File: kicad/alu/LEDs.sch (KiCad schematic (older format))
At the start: 114 parts

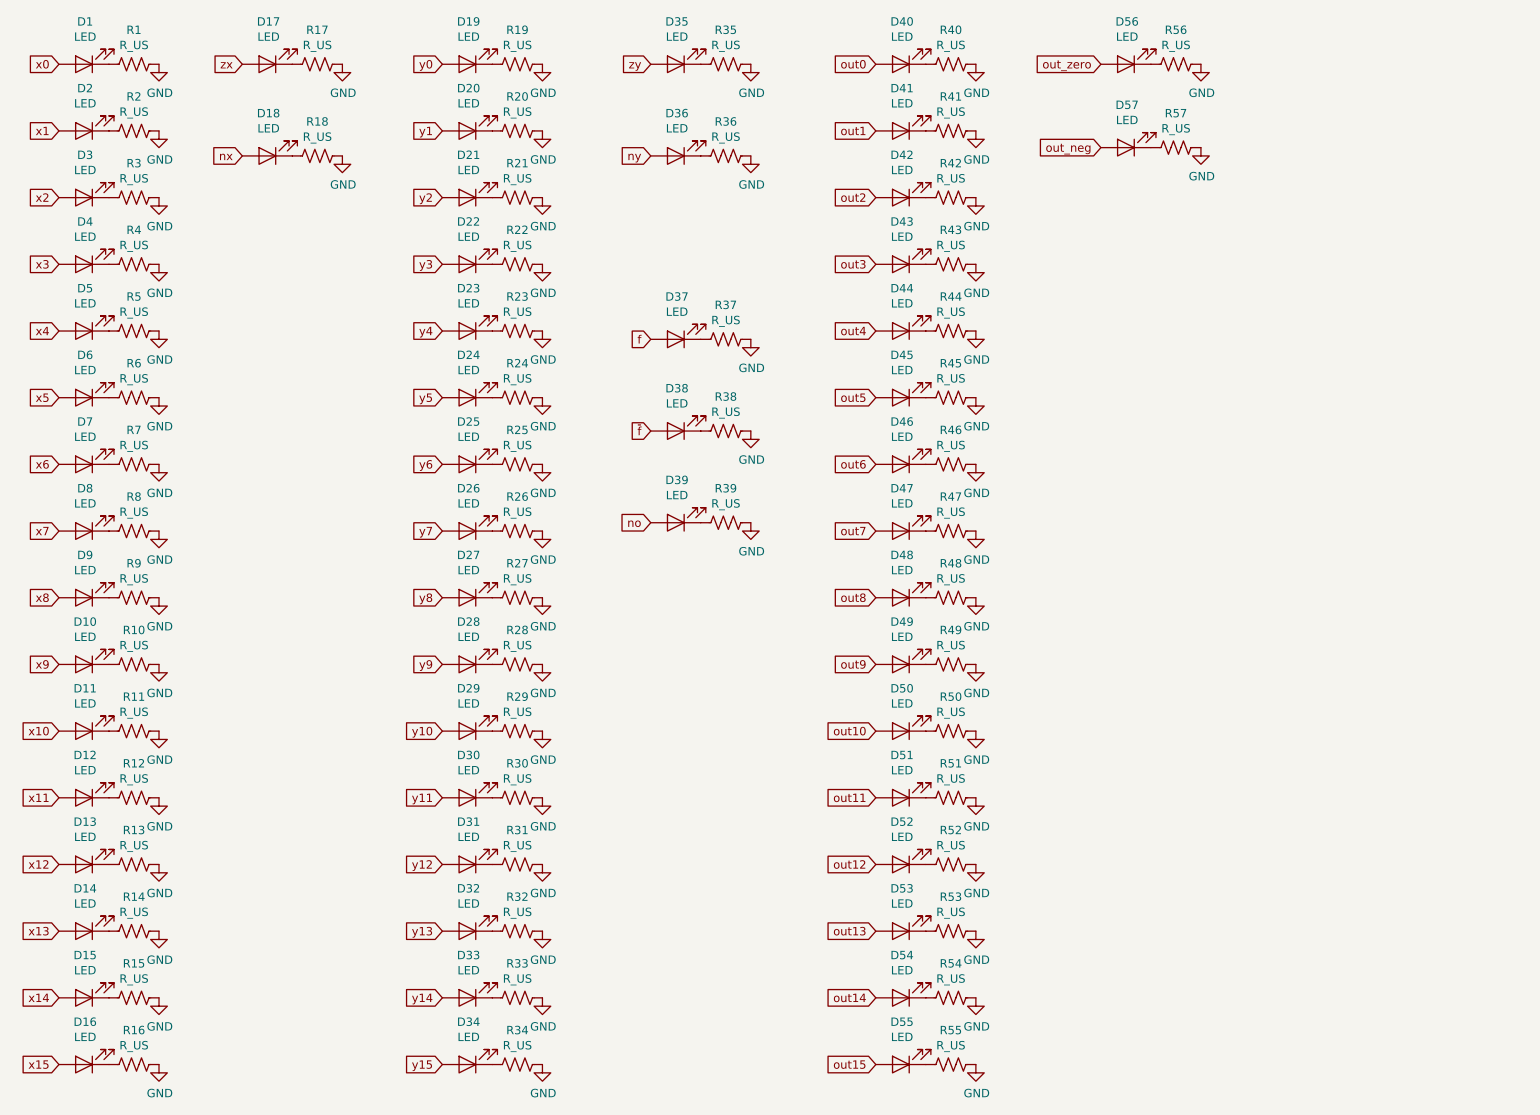
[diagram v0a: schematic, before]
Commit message: ALU schematic, layout, routing complete. Associated motherboardmod. Also added Load LED to register and program counter boards.
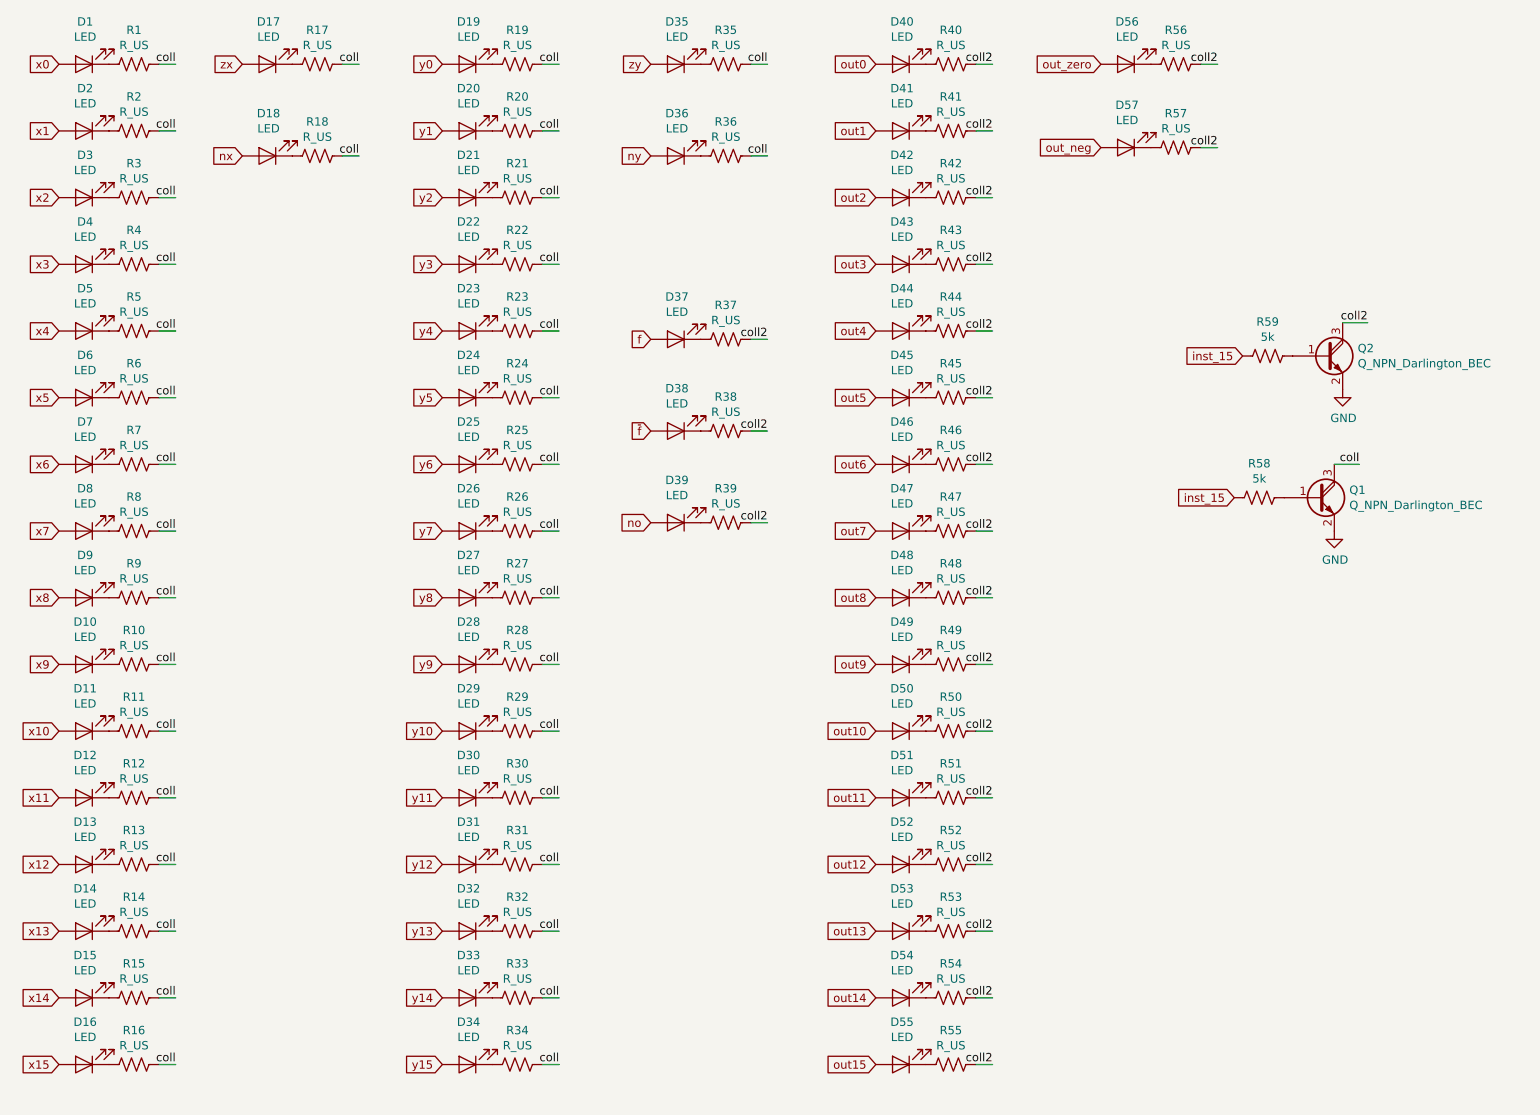
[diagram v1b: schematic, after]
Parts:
- added Q1, Q2: Q_NPN_Darlington_BEC, Package_TO_SOT_SMD:SOT-23, symbol Device:Q_NPN_Darlington_BEC
- added R58, R59: 5k, Resistor_SMD:R_1206_3216Metric, symbol Device:R_US
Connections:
- net GND: now also Q1.2 (E), Q2.2 (E); no longer R1.1, R10.1, R11.1, R12.1, R13.1, R14.1, R15.1, R16.1, R17.1, R18.1, R19.1, R2.1, R20.1, R21.1, R22.1, R23.1, R24.1, R25.1, R26.1, R27.1, R28.1, R29.1, R3.1, R30.1, R31.1, R32.1, R33.1, R34.1, R35.1, R36.1, R37.1, R38.1, R39.1, R4.1, R40.1, R41.1, R42.1, R43.1, R44.1, R45.1, R46.1, R47.1, R48.1, R49.1, R5.1, R50.1, R51.1, R52.1, R53.1, R54.1, R55.1, R56.1, R57.1, R6.1, R7.1, R8.1, R9.1
- new net: Q1.1 (B), R58.1
- new net: Q2.1 (B), R59.1
- new net coll: Q1.3 (C), R1.1, R10.1, R11.1, R12.1, R13.1, R14.1, R15.1, R16.1, R17.1, R18.1, R19.1, R2.1, R20.1, R21.1, R22.1, R23.1, R24.1, R25.1, R26.1, R27.1, R28.1, R29.1, R3.1, R30.1, R31.1, R32.1, R33.1, R34.1, R35.1, R36.1, R4.1, R5.1, R6.1, R7.1, R8.1, R9.1
- new net coll2: Q2.3 (C), R37.1, R38.1, R39.1, R40.1, R41.1, R42.1, R43.1, R44.1, R45.1, R46.1, R47.1, R48.1, R49.1, R50.1, R51.1, R52.1, R53.1, R54.1, R55.1, R56.1, R57.1
- new net inst_15: R58.2, R59.2

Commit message: Readme updates (#6)
* Readme intro section

* Board revisions for manufacturing, add digikey PNs to all, added logo.
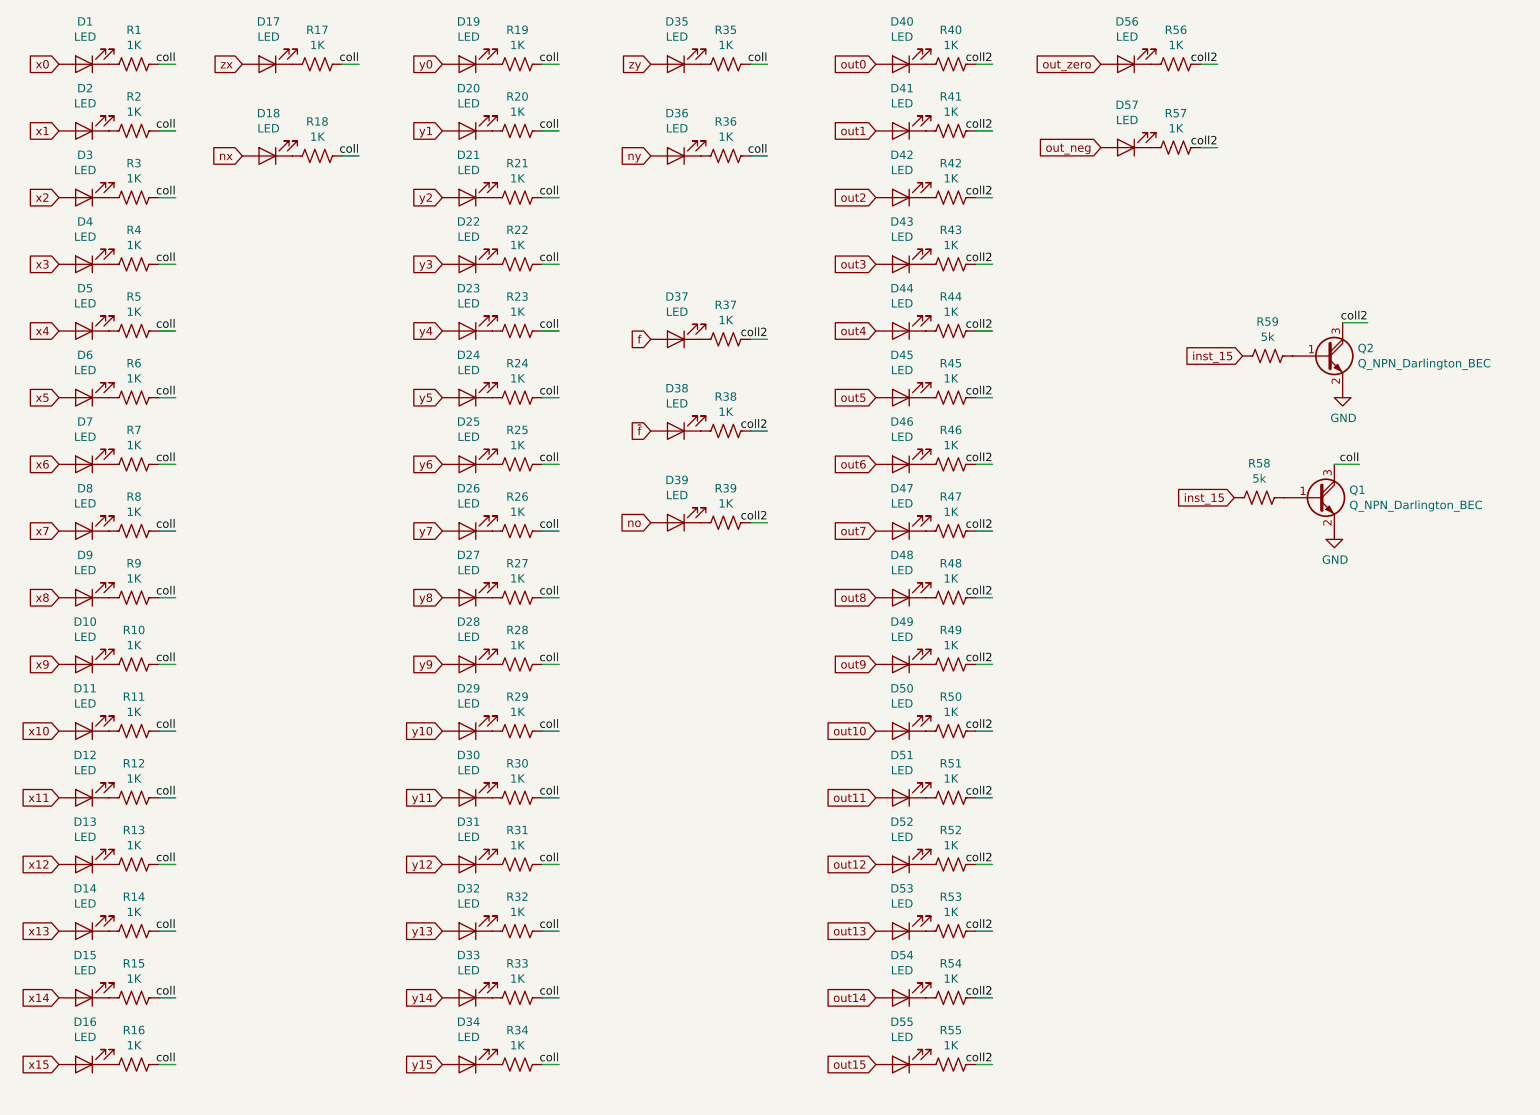
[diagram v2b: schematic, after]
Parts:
- R1, R10, R11, R12, R13, R14, R15, R16, R17, R18, R19, R2, R20, R21, R22, R23, R24, R25, R26, R27, R28, R29, R3, R30, R31, R32, R33, R34, R35, R36, R37, R38, R39, R4, R40, R41, R42, R43, R44, R45, R46, R47, R48, R49, R5, R50, R51, R52, R53, R54, R55, R56, R57, R6, R7, R8, R9: value R_US -> 1K; Digikey PN (none) -> P1.0KECT-ND
- R58, R59: Digikey PN (none) -> P5.1KECT-ND
